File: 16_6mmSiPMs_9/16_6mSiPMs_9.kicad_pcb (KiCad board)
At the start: 2 copper layers, 85.8 x 50.8 mm, 50 parts

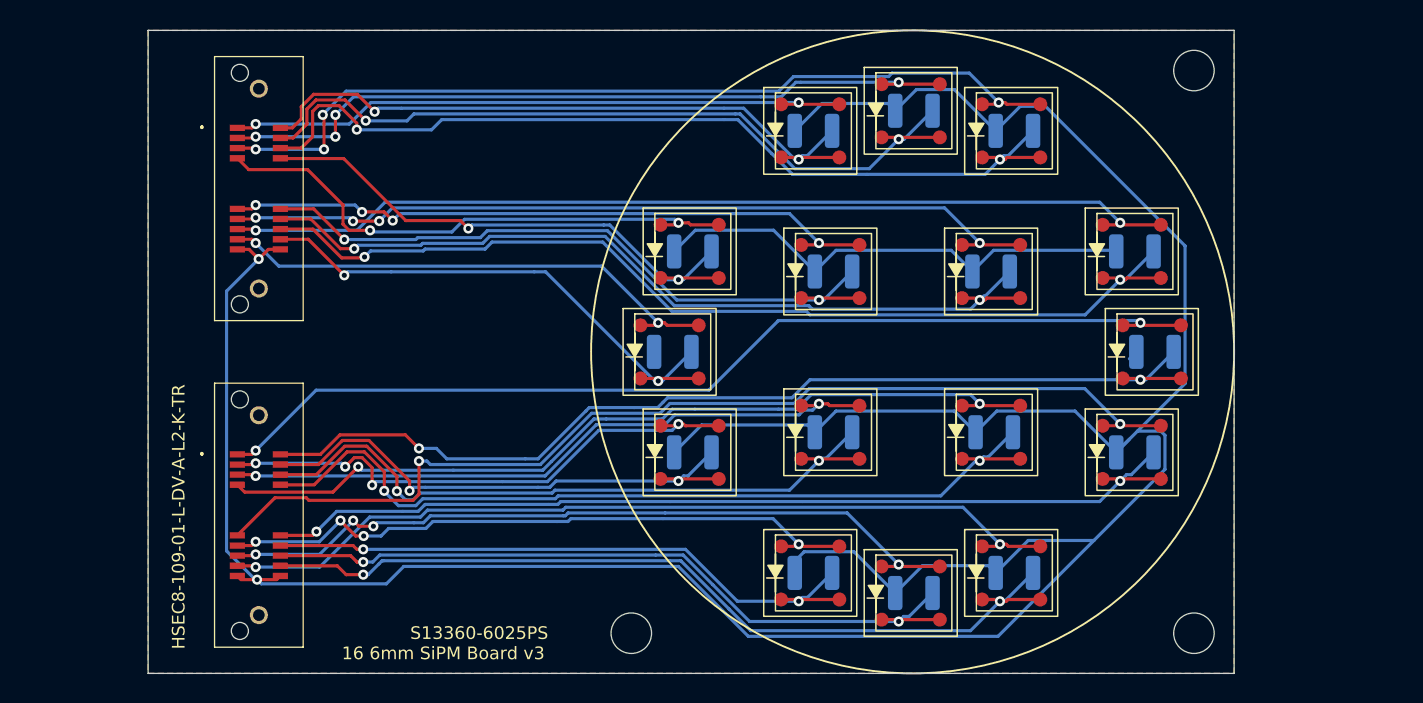
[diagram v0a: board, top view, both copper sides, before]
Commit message: Updated PCBs to include temp sensors
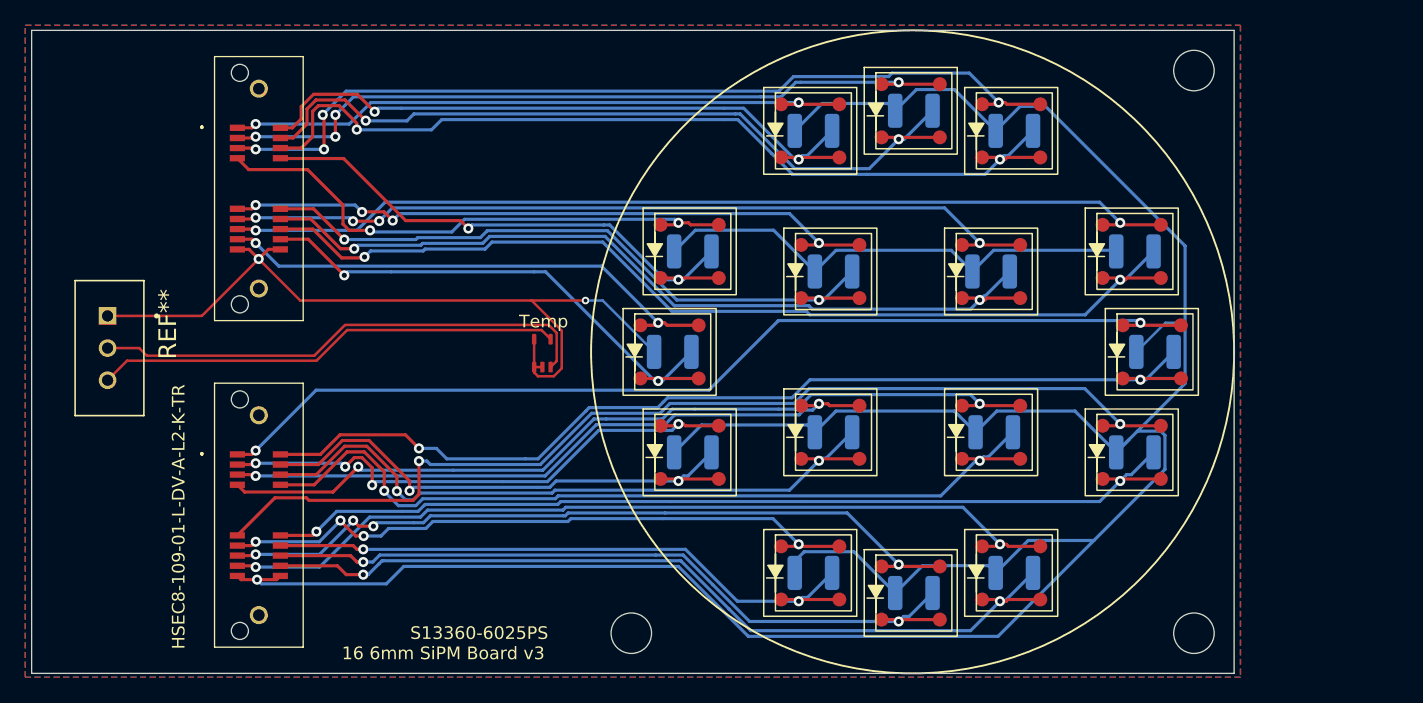
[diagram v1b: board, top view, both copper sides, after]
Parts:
- added ?: , , F.Cu at (195.0, 104.0)
- added ?: , , F.Cu at (195.0, 101.8)
- added ?: , , F.Cu at (194.3, 104.0)
- added ?: , , F.Cu at (193.7, 104.0)
- added ?: , , F.Cu at (193.7, 101.8)
- added REF**: TE_103414-1, AMPMODU:TE_103414-1, F.Cu at (160.0, 102.5)
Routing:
- net TMP_OUT: track 0.00 -> 39.9 mm
- net TMP_VDD: track 0.00 -> 36.9 mm
- net GND: track 287.5 -> 324.3 mm, vias 2 -> 3
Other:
- board size 85.8 x 50.8 mm -> 95 x 50.8 mm
- board text added: "Temp"

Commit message: Adding boards
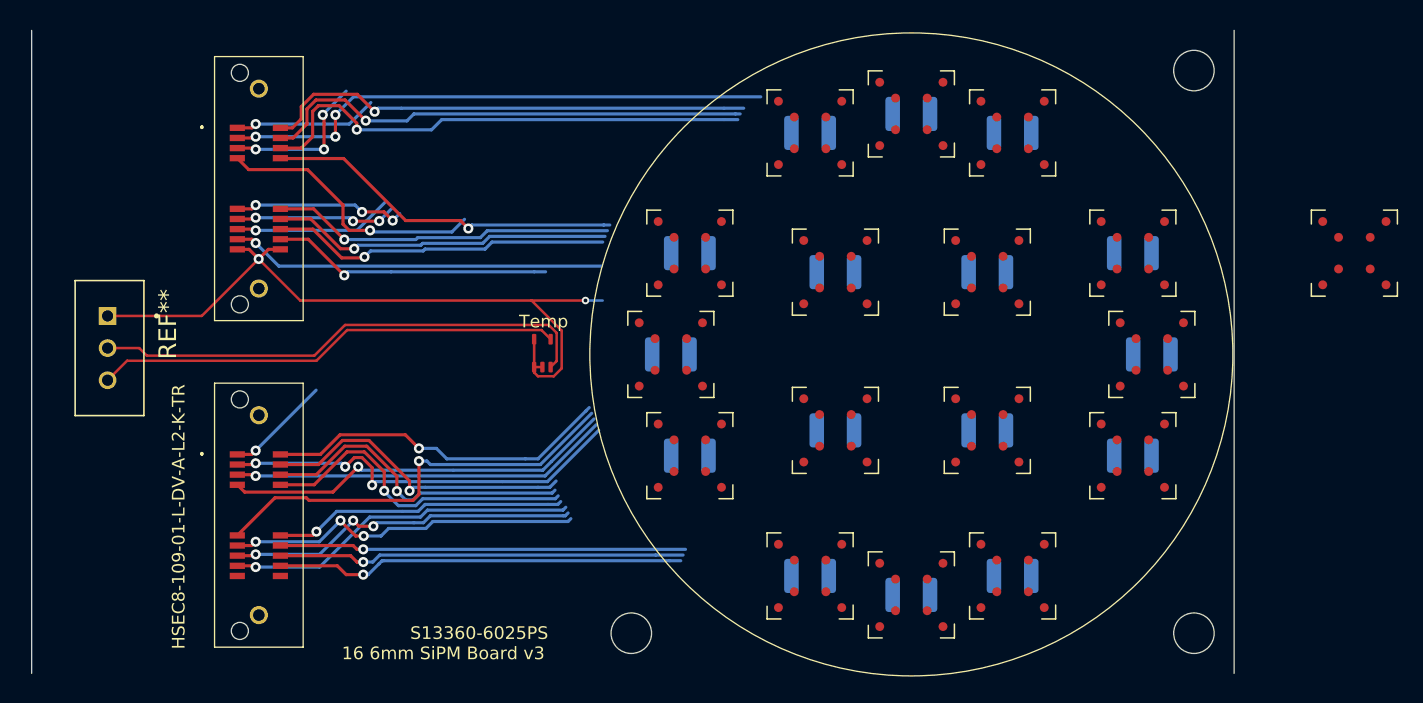
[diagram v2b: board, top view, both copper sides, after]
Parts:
- removed the REF** at (220.7, 121.8)
- removed the REF** at (239.8, 102.8)
- removed the REF** at (238.2, 94.9)
- removed the REF** at (228.6, 85.3)
- removed the REF** at (212.8, 85.3)
- removed the REF** at (214.3, 109.2)
- removed the REF** at (212.8, 120.3)
- removed the REF** at (203.2, 110.7)
- removed the REF** at (214.3, 96.5)
- removed the REF** at (228.6, 120.3)
- removed the REF** at (203.2, 94.9)
- removed the REF** at (220.7, 83.8)
- removed the REF** at (227.1, 96.5)
- removed the REF** at (201.7, 102.8)
- removed the REF** at (238.2, 110.7)
- removed the REF** at (227.1, 109.2)
- removed REF**10 (x16): S13360-6025PE, SiPM:S13360-6025PE
- added REF**: Hamamatsu_S14160-6050HS, OptoDevice:Hamamatsu_S14160-6050HS, F.Cu at (258.5, 95.0)
- added REF**: Hamamatsu_S14160-6050HS, OptoDevice:Hamamatsu_S14160-6050HS, F.Cu at (241.0, 111.0)
- added REF**: Hamamatsu_S14160-6050HS, OptoDevice:Hamamatsu_S14160-6050HS, F.Cu at (231.5, 120.5)
- added REF**: Hamamatsu_S14160-6050HS, OptoDevice:Hamamatsu_S14160-6050HS, F.Cu at (242.5, 103.0)
- added REF**: Hamamatsu_S14160-6050HS, OptoDevice:Hamamatsu_S14160-6050HS, F.Cu at (217.5, 96.5)
- added REF**: Hamamatsu_S14160-6050HS, OptoDevice:Hamamatsu_S14160-6050HS, F.Cu at (215.5, 120.5)
- added REF**: Hamamatsu_S14160-6050HS, OptoDevice:Hamamatsu_S14160-6050HS, F.Cu at (229.5, 109.0)
- added REF**: Hamamatsu_S14160-6050HS, OptoDevice:Hamamatsu_S14160-6050HS, F.Cu at (206.0, 95.0)
- added REF**: Hamamatsu_S14160-6050HS, OptoDevice:Hamamatsu_S14160-6050HS, F.Cu at (217.5, 109.0)
- added REF**: Hamamatsu_S14160-6050HS, OptoDevice:Hamamatsu_S14160-6050HS, F.Cu at (206.0, 111.0)
- added REF**: Hamamatsu_S14160-6050HS, OptoDevice:Hamamatsu_S14160-6050HS, F.Cu at (215.5, 85.5)
- added REF**: Hamamatsu_S14160-6050HS, OptoDevice:Hamamatsu_S14160-6050HS, F.Cu at (229.5, 96.5)
- added REF**: Hamamatsu_S14160-6050HS, OptoDevice:Hamamatsu_S14160-6050HS, F.Cu at (241.0, 95.0)
- added REF**: Hamamatsu_S14160-6050HS, OptoDevice:Hamamatsu_S14160-6050HS, F.Cu at (204.5, 103.0)
- added REF**: Hamamatsu_S14160-6050HS, OptoDevice:Hamamatsu_S14160-6050HS, F.Cu at (223.5, 84.0)
- added REF**: Hamamatsu_S14160-6050HS, OptoDevice:Hamamatsu_S14160-6050HS, F.Cu at (223.5, 122.0)
- added REF**: Hamamatsu_S14160-6050HS, OptoDevice:Hamamatsu_S14160-6050HS, F.Cu at (231.5, 85.5)
- moved 10 nF 0.57 mm to (229.5, 109.0)
- moved 10 nF 0.35 mm to (206.0, 111.0)
- moved 10 nF 0.35 mm to (215.5, 120.5)
- moved 10 nF 0.32 mm to (242.5, 103.0)
- moved 10 nF 0.32 mm to (223.5, 84.0)
- moved 10 nF 0.31 mm to (241.0, 111.0)
- moved 10 nF 0.31 mm to (215.5, 85.5)
- moved 10 nF 0.30 mm to (229.5, 96.5)
- moved 10 nF 0.27 mm to (206.0, 95.0)
- moved 10 nF 0.27 mm to (231.5, 120.5)
- moved 10 nF 0.25 mm to (204.5, 103.0)
- moved 10 nF 0.25 mm to (223.5, 122.0)
- moved 10 nF 0.21 mm to (241.0, 95.0)
- moved 10 nF 0.21 mm to (231.5, 85.5)
- moved 10 nF 0.21 mm to (217.5, 109.0)
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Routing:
- net GND: track 324.3 -> 58.5 mm, vias 3 -> 2
- net 8C: track 80.6 -> 8.33 mm, vias 2 -> 1
- net 6C: track 76.1 -> 12.6 mm, vias 2 -> 1
- net 2C: track 70.1 -> 12.3 mm, vias 4 -> 3
- net 12A: track 76.4 -> 23.3 mm, vias 2 -> 1
- net 6A: track 79.7 -> 27.0 mm, vias 2 -> 1
- net 8A: track 80.2 -> 27.5 mm, vias 2 -> 1
- net 5C: track 65.1 -> 12.8 mm, vias 4 -> 3
- net 12C: track 82.4 -> 33.9 mm, vias 2 -> 1
- net 11A: track 68.8 -> 26.0 mm, vias 2 -> 1
- net 5A: track 67.3 -> 27.0 mm, vias 2 -> 1
- net 15C: track 68.2 -> 27.9 mm, vias 2 -> 1
- net 4C: track 52.5 -> 13.7 mm, vias 4 -> 3
- net 0C: track 49.9 -> 11.4 mm, vias 2 -> 1
- net 15A: track 69.1 -> 32.4 mm, vias 2 -> 1
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- removed copper zone on B.Cu, net (none)
- removed copper zone on F.Cu, net (none)
